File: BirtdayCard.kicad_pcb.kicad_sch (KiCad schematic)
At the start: 54 parts, among them J1 Conn_01x04_Socket, J2 Conn_01x05_Pin, J3 USB_C_Receptacle_USB2.0, Q1 2N7002_C306856, U1 ESP32-C3-WROOM-02-N4(4MB), U2 AMS1117-3.3_C347222

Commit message: board improvements and added media
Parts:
- removed J3: USB_C_Receptacle_USB2.0, easyeda2kicad:TYPE-C-SMD_TYPE-C-6P_5, symbol Connector:USB_C_Receptacle_USB2.0
- added USB1: TYPE-C 6P(073), easyeda2kicad:TYPE-C-SMD_TYPE-C-6P_5, symbol easyeda2kicad:TYPE-C6P(073)
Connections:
- net GND: now also USB1.7 (EH), USB1.A12 (GND), USB1.B12 (GND)
- net at F1.1: now also USB1.A9 (VBUS), USB1.B9 (VBUS)
- net at R16.2: now also USB1.A5 (CC1)
- net at R13.2: now also USB1.B5 (CC2)
- no-connect marks 3 -> 1
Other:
- note added: "POWER IN"
- note removed: "POWER IN + USBDATA"
- moved on the sheet: D6, F1

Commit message: Improved silkscreen and text
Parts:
- removed USB1: TYPE-C 6P(073), easyeda2kicad:TYPE-C-SMD_TYPE-C-6P_5, symbol easyeda2kicad:TYPE-C6P(073)
- added USB1: TYPE-C16PIN, easyeda2kicad:USB-C-SMD_TYPE-C16PIN, symbol easyeda2kicad:TYPE-C16PIN
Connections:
- net +3V3: no longer C32.1, C33.1, D10.1 (VDD), D11.1 (VDD), D12.1 (VDD), D13.1 (VDD), D14.1 (VDD), D15.1 (VDD), D16.1 (VDD), D17.1 (VDD), D18.1 (VDD), D19.1 (VDD), D20.1 (VDD), D21.1 (VDD), D22.1 (VDD), D23.1 (VDD), D24.1 (VDD), D25.1 (VDD), D26.1 (VDD), D27.1 (VDD)
- net +5V: now also C32.1, C33.1, D10.1 (VDD), D11.1 (VDD), D12.1 (VDD), D13.1 (VDD), D14.1 (VDD), D15.1 (VDD), D16.1 (VDD), D17.1 (VDD), D18.1 (VDD), D19.1 (VDD), D20.1 (VDD), D21.1 (VDD), D22.1 (VDD), D23.1 (VDD), D24.1 (VDD), D25.1 (VDD), D26.1 (VDD), D27.1 (VDD)
- net D+_USB: now also USB1.A6 (DP1), USB1.B6 (DP2)
- net D-_USB: now also USB1.A7 (DN1), USB1.B7 (DN2)
- net GND: now also USB1.1 (SHELL), USB1.2 (SHELL), USB1.3 (SHELL), USB1.4 (SHELL), USB1.A1B12 (GND), USB1.B1A12 (GND)
- net GPIO0: now also J2.3 (Pin_3); no longer J2.5 (Pin_5)
- net GPIO2: now also J2.5 (Pin_5); no longer J2.3 (Pin_3)
- net at F1.1: now also USB1.A4B9 (VBUS), USB1.B4A9 (VBUS)
- net at R16.2: now also USB1.A5 (CC1)
- net at R13.2: now also USB1.B5 (CC2)
- no-connect marks 1 -> 3
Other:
- note added: "POWER + DATA IN"
- note removed: "POWER IN"
- moved on the sheet: R13, R16

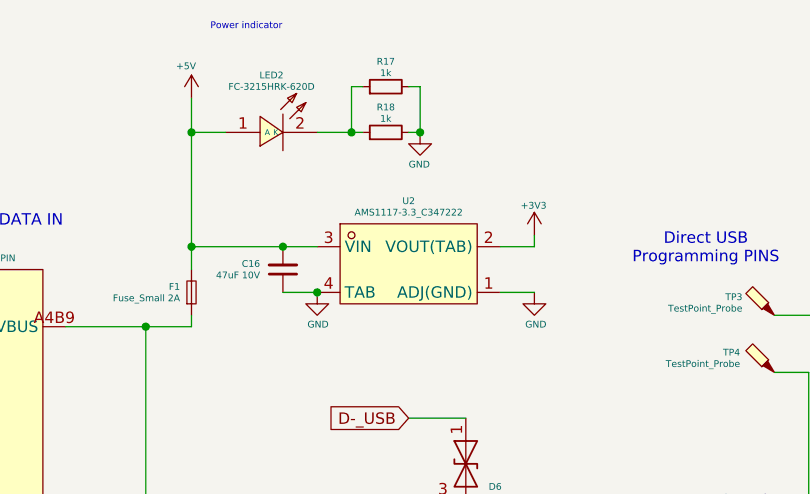
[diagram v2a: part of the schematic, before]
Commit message: Updated schematic and PCB (resistor removed)
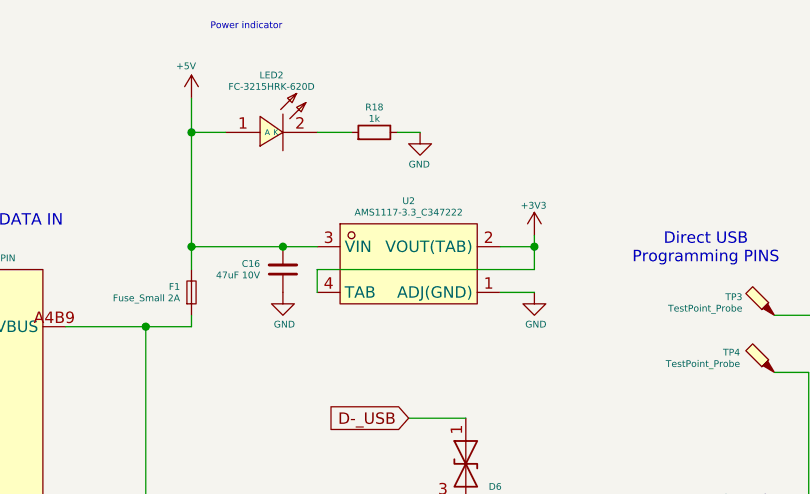
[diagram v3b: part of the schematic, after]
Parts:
- removed R17: 1k, Resistor_SMD:R_1206_3216Metric_Pad1.30x1.75mm_HandSolder, symbol Device:R_Small
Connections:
- net +3V3: now also U2.4 (TAB)
- net GND: no longer U2.4 (TAB)
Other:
- moved on the sheet: R18
